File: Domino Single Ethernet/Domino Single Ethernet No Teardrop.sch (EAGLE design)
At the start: 12 parts, among them J1 MH6-1, J2 FR04-2, J3 B50(27-51)FP4-151-A613-B12

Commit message: Changed copyright
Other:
- note added: "The Domino Team may make changes to specifications and product"
- note added: "© 2014, The Domino Team All rights reserved."
- note removed: "Michel Stempin may make changes to specifications and product"
- note removed: "© 2014, Michel Stempin All rights reserved."
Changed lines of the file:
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@@
 <text x="302.26" y="12.7" size="0.8128" layer="94">Reference designs are provided "AS IS" and "WITH ALL FAULTS".</text>
 <text x="302.26" y="10.16" size="0.8128" layer="94">regarding this product, including but not limited to, any implied warranties of</text>
-<text x="302.26" y="6.35" size="0.8128" layer="94">Michel Stempin may make changes to specifications and product </text>
+<text x="302.26" y="6.35" size="0.8128" layer="94">The Domino Team may make changes to specifications and product </text>
 <text x="302.26" y="11.43" size="0.8128" layer="94">Global Marine Networks disclaims all other warranties express or implied, </text>
 <text x="302.26" y="8.89" size="0.8128" layer="94">merchantibility or fitness for any particular application.</text>
@@
 <text x="256.54" y="7.62" size="1.778" layer="94" align="center">Domino
 Qi</text>
-<text x="345.44" y="20.32" size="1.27" layer="94">© 2014, Michel Stempin
+<text x="345.44" y="20.32" size="1.27" layer="94">© 2014, The Domino Team
 All rights reserved.</text>
 <text x="379.222" y="5.334" size="1.778" layer="94">&gt;REV</text>

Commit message: ... and all the files I missed
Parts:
- removed C5, C7: 100n, Domino:CAP_0402
- added C2: 100n, Domino:CAP_0402
- added C3: 2n2, Domino:CAP_1206
- added D1: BLUE, Domino:LED_0603
- added D2: WHITE, Domino:LED_0603
- added D3, D4, D5, D6: GREEN, Domino:LED_0603
- added D7: RED, Domino:LED_0603
- added D8: ORANGE, Domino:LED_0603
- added D9: YELLOW, Domino:LED_0603
- added R1, R2, R3, R4: 49R9, Domino:RES_0402
- added R10, R11, R9: 270R, Domino:RES_0603
- added R12: 150R, Domino:RES_0603
- added R13, R14: 330R, Domino:RES_0603
- C1: value 2n2 -> 100n; device Domino:CAP_1206 -> Domino:CAP_0402; PARTNO C1210_2n2_X7R_10%_CER_2kV -> C0402_100n_X7R_10%_CER_50V; VOLT 2kV -> 50V
- J1: value MH6-1 -> MH18-1; device Domino:MH6-1 -> Domino:MH18-1; PARTNO MH6-1-0.1 -> MH18-1-0.1
- J2: value FR04-2 -> MH18-1; device Domino:FR04-2 -> Domino:MH18-1; PARTNO FR04-2-0.1 -> MH18-1-0.1
- R5: value 49R9 -> 330R; device Domino:RES_0402 -> Domino:RES_0603; PARTNO R0402_49R9_1%_62.5mW -> R0603_330R_5%_125mW; TOL 1% -> 5%
- R6, R7, R8: value 49R9 -> 270R; device Domino:RES_0402 -> Domino:RES_0603; PARTNO R0402_49R9_1%_62.5mW -> R0603_270R_5%_125mW; RATE 62.5mW -> 125mW; TOL 1% -> 5%
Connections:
- removed net P4_LED_L_A: J2.6, J3.13
- removed net P4_LED_L_C: J2.8, J3.14
- removed net P4_LED_R_A: J2.2, J3.11
- removed net P4_LED_R_C: J2.4, J3.12
- removed net VC12: J2.5, J3.9
- removed net VC36: J2.7, J3.10
- removed net VC45: J2.1, J3.4
- removed net VC78: J2.3, J3.5
- new net +3V3: D7.A, D8.A, D9.A, J1.8, J3.13, R5.2
- new net GREEN_LED: J3.11, R5.1
- new net LAN1_LED: D3.A, R8.2
- new net LAN2_LED: D4.A, R9.2
- new net LAN3_LED: D5.A, R10.2
- new net LAN4_LED: D6.A, R11.2
- new net LED0: J1.9, R6.1
- new net LED1: J1.10, R7.1
- new net LED2: J1.11, R8.1
- new net LED3: J1.12, R9.1
- new net LED4: J1.13, R10.1
- new net LED5: J1.14, R11.1
- new net LED6: J1.15, R12.1
- new net LED7: J1.16, R13.1
- new net LED8: J1.17, R14.1
- new net SYS_LED: D8.C, R13.2
- new net USB_LED: D2.A, R7.2
- new net WAN_LED: D7.C, J3.14, R12.2
- new net WLAN_LED: D1.A, R6.2
- new net WPS_LED: D9.C, R14.2
- net +2VA_ETH_OUT: now also C4.2, J2.14; no longer C7.2, J1.6
- net GND: now also C2.1, C3.1, D1.C, D2.C, D3.C, D4.C, D5.C, D6.C, J1.18, J2.9, J3.12; no longer C5.1, C7.1, J1.1
- net P4_RX: now also C1.2, R1.1, R2.1; no longer C4.2, R5.1, R6.1
- net P4_RX_N: now also J2.11, R2.2; no longer J1.3, R6.2
- net P4_RX_P: now also J2.10, R1.2; no longer J1.2, R5.2
- net P4_TX: now also C2.2, R3.1, R4.1; no longer C5.2, R7.1, R8.1
- net P4_TX_N: now also J2.13, R4.2; no longer J1.5, R8.2
- net P4_TX_P: now also J2.12, R3.2; no longer J1.4, R7.2
- net SHIELD: now also C3.2; no longer C1.2
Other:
- note added: "LAN1"
- note added: "LAN2"
- note added: "LAN3"
- note added: "LAN4"
- note added: "SYS"
- note added: "USB"
- note added: "WAN"
- note added: "WLAN"
- note added: "WPS"
- note removed: "LEDS"
- note removed: "PoE"
- moved on the sheet: C1, C4, J3, R5, R6, R7, R8

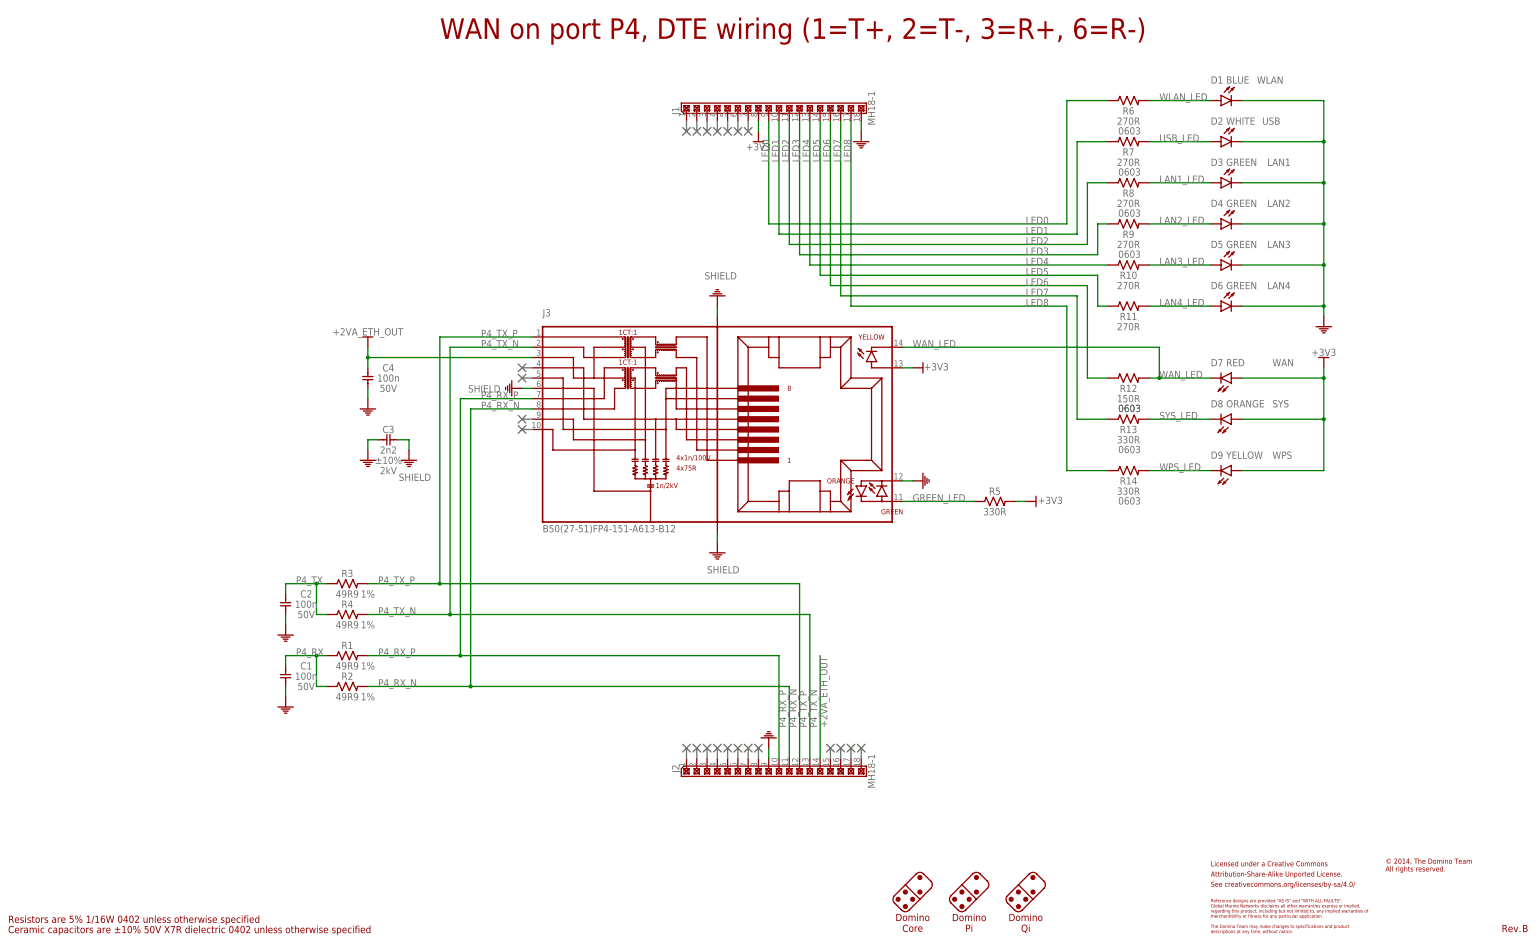
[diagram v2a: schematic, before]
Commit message: Domino Single Ethernet tile Revision B
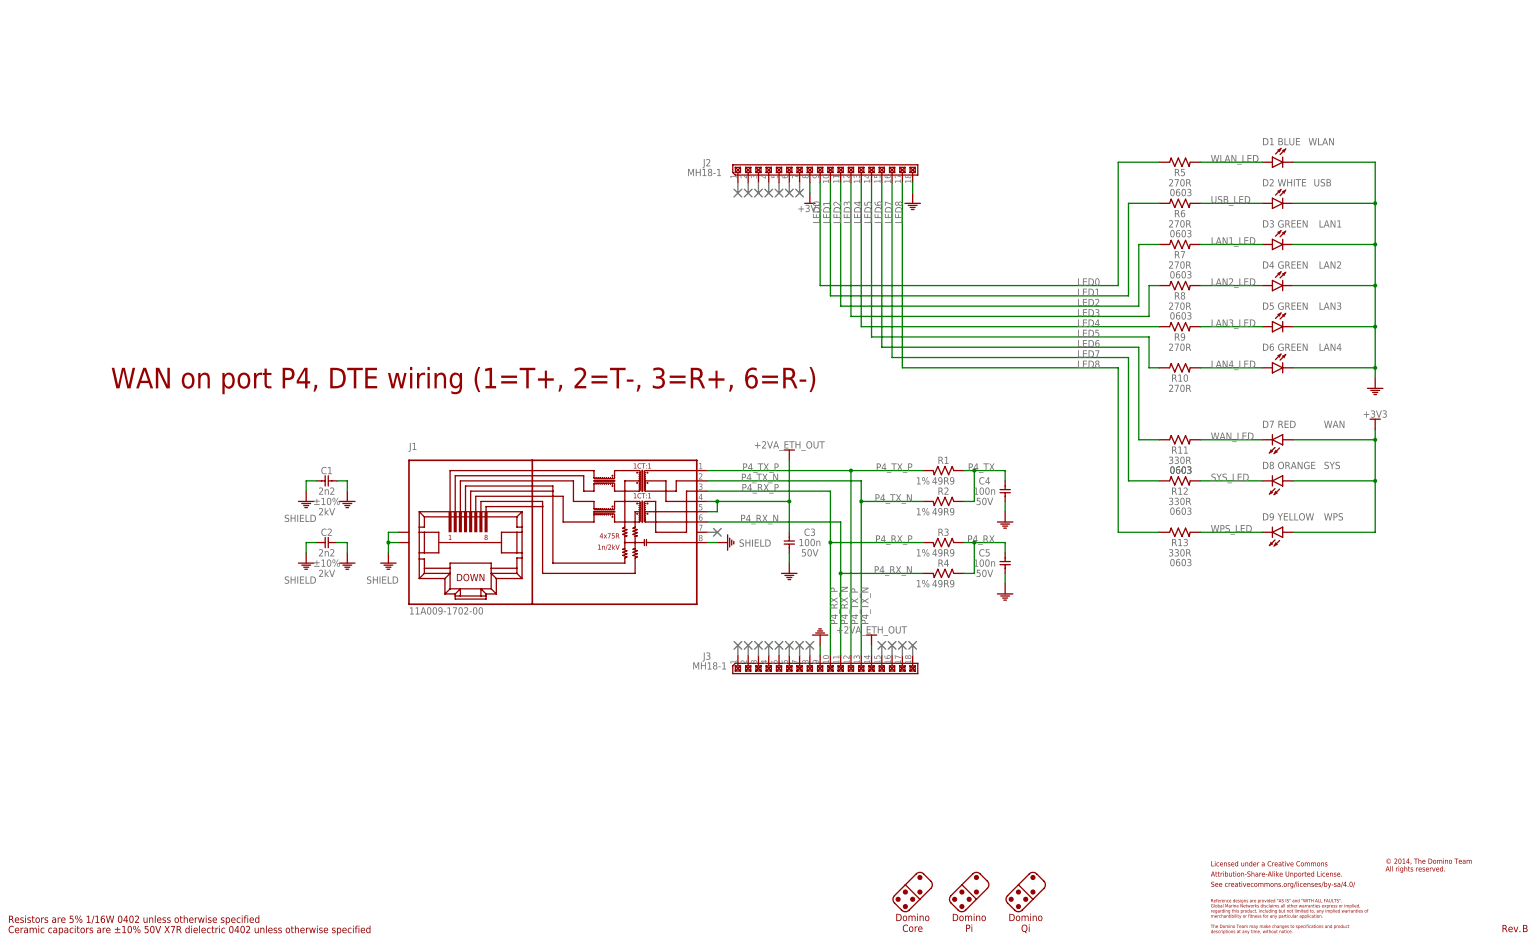
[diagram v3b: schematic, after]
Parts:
- removed R14: 330R, Domino:RES_0603
- added C5: 100n, Domino:CAP_0402
- C1, C2: value 100n -> 2n2; device Domino:CAP_0402 -> Domino:CAP_1206; PARTNO C0402_100n_X7R_10%_CER_50V -> C1210_2n2_X7R_10%_CER_2kV; VOLT 50V -> 2kV
- C3: value 2n2 -> 100n; device Domino:CAP_1206 -> Domino:CAP_0402; PARTNO C1210_2n2_X7R_10%_CER_2kV -> C0402_100n_X7R_10%_CER_50V; VOLT 2kV -> 50V
- J1: value MH18-1 -> 11A009-1702-00; device Domino:MH18-1 -> Domino:11A009-1702-00; PARTNO MH18-1-0.1 -> 11A009-1702-00
- J3: value B50(27-51)FP4-151-A613-B12 -> MH18-1; device Domino:B50(27-51)FP4-151-A613-B12 -> Domino:MH18-1; PARTNO B50(27-51)FP4-151-A613-B12 -> MH18-1-0.1
- R11: value 270R -> 330R; PARTNO R0603_270R_5%_125mW -> R0603_330R_5%_125mW
- R12: value 150R -> 330R; PARTNO R0603_150R_5%_125mW -> R0603_330R_5%_125mW
- R5: value 330R -> 270R; PARTNO R0603_330R_5%_125mW -> R0603_270R_5%_125mW; RATE 62.5mW -> 125mW
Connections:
- removed net GREEN_LED: J3.11, R5.1
- net +2VA_ETH_OUT: now also C3.2, J1.P4, J1.P5, J3.14; no longer C4.2, J2.14, J3.3
- net +3V3: now also J2.8; no longer J1.8, J3.13, R5.2
- net GND: now also C5.1, J2.18, J3.9; no longer J1.18, J2.9, J3.12
- net LAN1_LED: now also R7.2; no longer R8.2
- net LAN2_LED: now also R8.2; no longer R9.2
- net LAN3_LED: now also R9.2; no longer R10.2
- net LAN4_LED: now also R10.2; no longer R11.2
- net LED0: now also J2.9, R5.1; no longer J1.9, R6.1
- net LED1: now also J2.10, R6.1; no longer J1.10, R7.1
- net LED2: now also J2.11, R7.1; no longer J1.11, R8.1
- net LED3: now also J2.12, R8.1; no longer J1.12, R9.1
- net LED4: now also J2.13, R9.1; no longer J1.13, R10.1
- net LED5: now also J2.14, R10.1; no longer J1.14, R11.1
- net LED6: now also J2.15, R11.1; no longer J1.15, R12.1
- net LED7: now also J2.16, R12.1; no longer J1.16, R13.1
- net LED8: now also J2.17, R13.1; no longer J1.17, R14.1
- net P4_RX: now also C5.2, R3.1, R4.1; no longer C1.2, R1.1, R2.1
- net P4_RX_N: now also J1.P6, J3.11, R4.2; no longer J2.11, J3.8, R2.2
- net P4_RX_P: now also J1.P3, J3.10, R3.2; no longer J2.10, J3.7, R1.2
- net P4_TX: now also C4.2, R1.1, R2.1; no longer C2.2, R3.1, R4.1
- net P4_TX_N: now also J1.P2, J3.13, R2.2; no longer J2.13, J3.2, R4.2
- net P4_TX_P: now also J1.P1, J3.12, R1.2; no longer J2.12, J3.1, R3.2
- net SHIELD: now also C1.2, C2.2, J1.P8, J1.SHIELD@1, J1.SHIELD@2; no longer C3.2, J3.6, J3.SHIELD@1, J3.SHIELD@2
- net SYS_LED: now also R12.2; no longer R13.2
- net USB_LED: now also R6.2; no longer R7.2
- net WAN_LED: now also R11.2; no longer J3.14, R12.2
- net WLAN_LED: now also R5.2; no longer R6.2
- net WPS_LED: now also R13.2; no longer R14.2
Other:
- moved on the sheet: C1, C2, C3, C4, D1, D2, D3, D4, D5, D6, D7, D8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

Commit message: Domino Single Ethernet Rev. C: changed Logos
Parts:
- added U$10: DOMINO_LOGO, Domino:DOMINO_LOGO
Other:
- note removed: "Domino Core"
- note removed: "Domino Pi"
- note removed: "Domino Qi"
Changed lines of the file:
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@@
 <layer number="54" name="bGND_GNDA" color="1" fill="9" visible="no" active="no"/>
 <layer number="56" name="wert" color="7" fill="1" visible="no" active="no"/>
+<layer number="90" name="Modules" color="5" fill="1" visible="yes" active="yes"/>
 <layer number="91" name="Nets" color="2" fill="1" visible="yes" active="yes"/>
 <layer number="92" name="Busses" color="1" fill="1" visible="yes" active="yes"/>
@@
 <layer number="143" name="mvRestrict" color="7" fill="1" visible="no" active="no"/>
 <layer number="144" name="Drill_legend" color="7" fill="1" visible="yes" active="yes"/>
+<layer number="145" name="DrillLegend_01-16" color="2" fill="9" visible="yes" active="yes"/>
+<layer number="146" name="DrillLegend_01-20" color="3" fill="9" visible="yes" active="yes"/>
 <layer number="147" name="Measures_X8" color="7" fill="1" visible="yes" active="yes"/>
 <layer number="148" name="mDocument" color="7" fill="1" visible="no" active="no"/>
 <layer number="149" name="mReference" color="7" fill="1" visible="no" active="no"/>
+<layer number="150" name="Pinout" color="7" fill="1" visible="yes" active="yes"/>
 <layer number="151" name="HeatSink" color="7" fill="1" visible="yes" active="yes"/>
 <layer number="152" name="mbDocu" color="7" fill="1" visible="no" active="no"/>
@@
 <attribute name="DATABASE" value="./../Common/BOM/Domino_DB.txt"/>
 <attribute name="DRAWN" value="M.STEMPIN"/>
-<attribute name="REV" value="B"/>
+<attribute name="REV" value="C"/>
 </attributes>
 <variantdefs>
@@
 <part name="PORT17" library="Domino" deviceset="NC" device=""/>
 <part name="PORT20" library="Domino" deviceset="NC" device=""/>
+<part name="U$10" library="Domino" deviceset="DOMINO_LOGO" device=""/>
 </parts>
 <sheets>
@@
 <text x="302.26" y="8.89" size="0.8128" layer="94">merchantibility or fitness for any particular application.</text>
 <text x="302.26" y="5.08" size="0.8128" layer="94">descriptions at any time, without notice.</text>
-<wire x1="238.079875" y1="14.341975" x2="240.77395" y2="17.036053125" width="0.1016" layer="94"/>
-<wire x1="240.77395" y1="17.036053125" x2="243.468028125" y2="19.730128125" width="0.1016" layer="94"/>
-<wire x1="243.468028125" y1="19.730128125" x2="245.264078125" y2="19.730128125" width="0.1016" layer="94" curve="-90"/>
-<wire x1="245.264078125" y1="19.730128125" x2="247.060128125" y2="17.934078125" width="0.1016" layer="94"/>
-<wire x1="247.060128125" y1="17.934078125" x2="247.060128125" y2="16.138028125" width="0.1016" layer="94" curve="-90"/>
-<wire x1="247.060128125" y1="16.138028125" x2="244.366053125" y2="13.44395" width="0.1016" layer="94"/>
-<wire x1="244.366053125" y1="13.44395" x2="241.671975" y2="10.749875" width="0.1016" layer="94"/>
-<wire x1="241.671975" y1="10.749875" x2="239.875925" y2="10.749875" width="0.1016" layer="94" curve="-90"/>
-<wire x1="239.875925" y1="10.749875" x2="238.079875" y2="12.545925" width="0.1016" layer="94"/>
-<wire x1="238.079875" y1="12.545925" x2="238.079875" y2="14.341975" width="0.1016" layer="94" curve="-90"/>
-<wire x1="240.77395" y1="17.036053125" x2="244.366053125" y2="13.44395" width="0.1016" layer="94"/>
-<circle x="238.9779" y="13.44395" radius="0.635" width="0" layer="94"/>
-<circle x="240.77395" y="15.240003125" radius="0.635" width="0" layer="94"/>
-<circle x="240.77395" y="11.6479" radius="0.635" width="0" layer="94"/>
-<circle x="242.57" y="13.44395" radius="0.635" width="0" layer="94"/>
-<circle x="244.366053125" y="15.24" radius="0.635" width="0" layer="94"/>
-<circle x="244.366053125" y="18.832103125" radius="0.635" width="0" layer="94"/>
-<wire x1="224.109875" y1="14.341975" x2="226.80395" y2="17.036053125" width="0.1016" layer="94"/>
-<wire x1="226.80395" y1="17.036053125" x2="229.498028125" y2="19.730128125" width="0.1016" layer="94"/>
-<wire x1="229.498028125" y1="19.730128125" x2="231.294078125" y2="19.730128125" width="0.1016" layer="94" curve="-90"/>
-<wire x1="231.294078125" y1="19.730128125" x2="233.090128125" y2="17.934078125" width="0.1016" layer="94"/>
-<wire x1="233.090128125" y1="17.934078125" x2="233.090128125" y2="16.138028125" width="0.1016" layer="94" curve="-90"/>
-<wire x1="233.090128125" y1="16.138028125" x2="230.396053125" y2="13.44395" width="0.1016" layer="94"/>
-<wire x1="230.396053125" y1="13.44395" x2="227.701975" y2="10.749875" width="0.1016" layer="94"/>
-<wire x1="227.701975" y1="10.749875" x2="225.905925" y2="10.749875" width="0.1016" layer="94" curve="-90"/>
-<wire x1="225.905925" y1="10.749875" x2="224.109875" y2="12.545925" width="0.1016" layer="94"/>
-<wire x1="224.109875" y1="12.545925" x2="224.109875" y2="14.341975" width="0.1016" layer="94" curve="-90"/>
-<wire x1="226.80395" y1="17.036053125" x2="230.396053125" y2="13.44395" width="0.1016" layer="94"/>
-<circle x="225.0079" y="13.44395" radius="0.635" width="0" layer="94"/>
-<circle x="226.80395" y="15.240003125" radius="0.635" width="0" layer="94"/>
-<circle x="226.80395" y="11.6479" radius="0.635" width="0" layer="94"/>
-<circle x="228.6" y="13.44395" radius="0.635" width="0" layer="94"/>
-<circle x="230.396053125" y="15.24" radius="0.635" width="0" layer="94"/>
-<circle x="230.396053125" y="18.832103125" radius="0.635" width="0" layer="94"/>
-<wire x1="252.049875" y1="14.341975" x2="254.74395" y2="17.036053125" width="0.1016" layer="94"/>
-<wire x1="254.74395" y1="17.036053125" x2="257.438028125" y2="19.730128125" width="0.1016" layer="94"/>
-<wire x1="257.438028125" y1="19.730128125" x2="259.234078125" y2="19.730128125" width="0.1016" layer="94" curve="-90"/>
-<wire x1="259.234078125" y1="19.730128125" x2="261.030128125" y2="17.934078125" width="0.1016" layer="94"/>
-<wire x1="261.030128125" y1="17.934078125" x2="261.030128125" y2="16.138028125" width="0.1016" layer="94" curve="-90"/>
-<wire x1="261.030128125" y1="16.138028125" x2="258.336053125" y2="13.44395" width="0.1016" layer="94"/>
-<wire x1="258.336053125" y1="13.44395" x2="255.641975" y2="10.749875" width="0.1016" layer="94"/>
-<wire x1="255.641975" y1="10.749875" x2="253.845925" y2="10.749875" width="0.1016" layer="94" curve="-90"/>
-<wire x1="253.845925" y1="10.749875" x2="252.049875" y2="12.545925" width="0.1016" layer="94"/>
-<wire x1="252.049875" y1="12.545925" x2="252.049875" y2="14.341975" width="0.1016" layer="94" curve="-90"/>
-<wire x1="254.74395" y1="17.036053125" x2="258.336053125" y2="13.44395" width="0.1016" layer="94"/>
-<circle x="252.9479" y="13.44395" radius="0.635" width="0" layer="94"/>
-<circle x="254.74395" y="15.240003125" radius="0.635" width="0" layer="94"/>
-<circle x="254.74395" y="11.6479" radius="0.635" width="0" layer="94"/>
-<circle x="256.54" y="13.44395" radius="0.635" width="0" layer="94"/>
-<circle x="258.336053125" y="15.24" radius="0.635" width="0" layer="94"/>
-<circle x="258.336053125" y="18.832103125" radius="0.635" width="0" layer="94"/>
-<text x="228.6" y="7.62" size="1.778" layer="94" align="center">Domino
-Core</text>
-<text x="242.57" y="7.62" size="1.778" layer="94" align="center">Domino
-Pi</text>
-<text x="256.54" y="7.62" size="1.778" layer="94" align="center">Domino
-Qi</text>
 <text x="345.44" y="20.32" size="1.27" layer="94">© 2014, The Domino Team
 All rights reserved.</text>
@@
 <instance part="PORT17" gate="G$1" x="226.06" y="76.2" rot="MR270"/>
 <instance part="PORT20" gate="G$1" x="228.6" y="76.2" rot="MR270"/>
+<instance part="U$10" gate="G$1" x="226.06" y="12.7"/>
 </instances>
 <busses>

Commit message: Domnio Single Ethernet Rev. D: changed silkscreen font ratio to 20%
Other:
- note added: "© 2014-2015, The Domino Team All rights reserved."
- note removed: "© 2014, The Domino Team All rights reserved."
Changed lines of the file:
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@@
 <text x="302.26" y="8.89" size="0.8128" layer="94">merchantibility or fitness for any particular application.</text>
 <text x="302.26" y="5.08" size="0.8128" layer="94">descriptions at any time, without notice.</text>
-<text x="345.44" y="20.32" size="1.27" layer="94">© 2014, The Domino Team
+<text x="345.44" y="20.32" size="1.27" layer="94">© 2014-2015, The Domino Team
 All rights reserved.</text>
 <text x="379.222" y="5.334" size="1.778" layer="94">&gt;REV</text>
